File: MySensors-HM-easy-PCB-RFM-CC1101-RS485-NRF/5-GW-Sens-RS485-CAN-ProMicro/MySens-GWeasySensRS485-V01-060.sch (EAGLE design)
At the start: 28 parts, among them IC1 LM1117MPX-ADJ, IC2 LD117ADT50TR, IC6 LM1117MPX-ADJ, X4 1751264

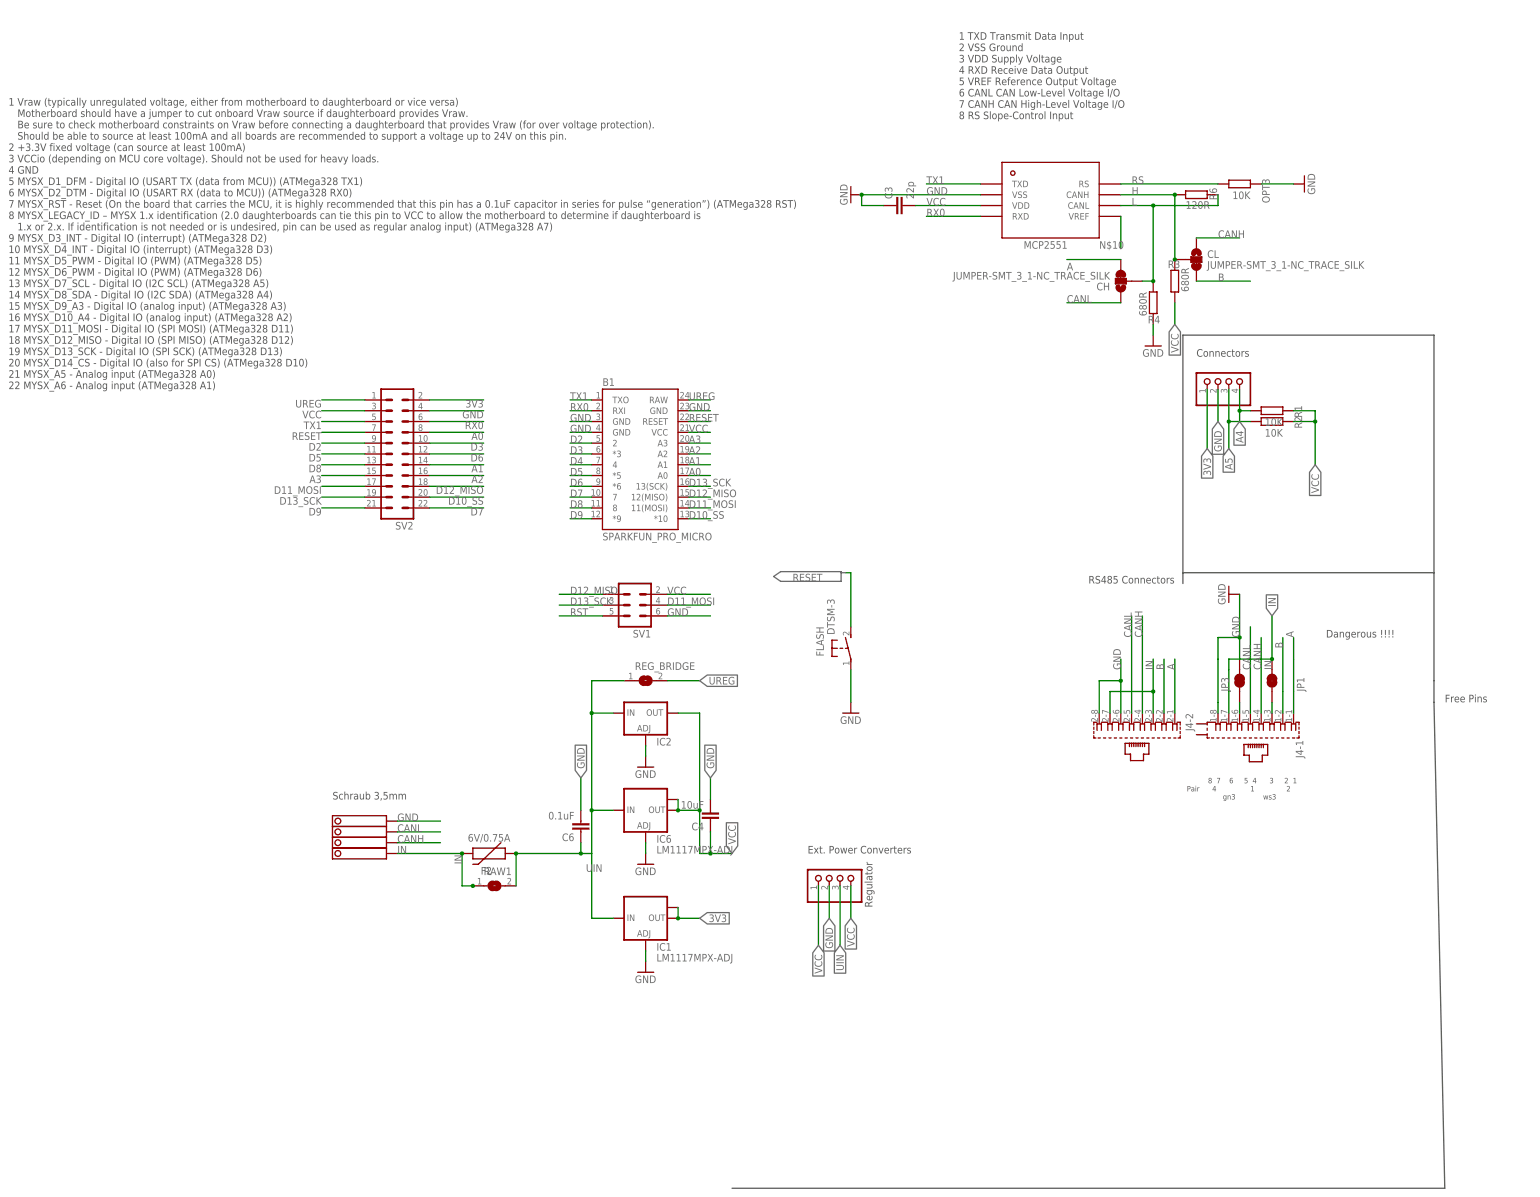
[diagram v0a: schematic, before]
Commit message: CAN/RS485 Board
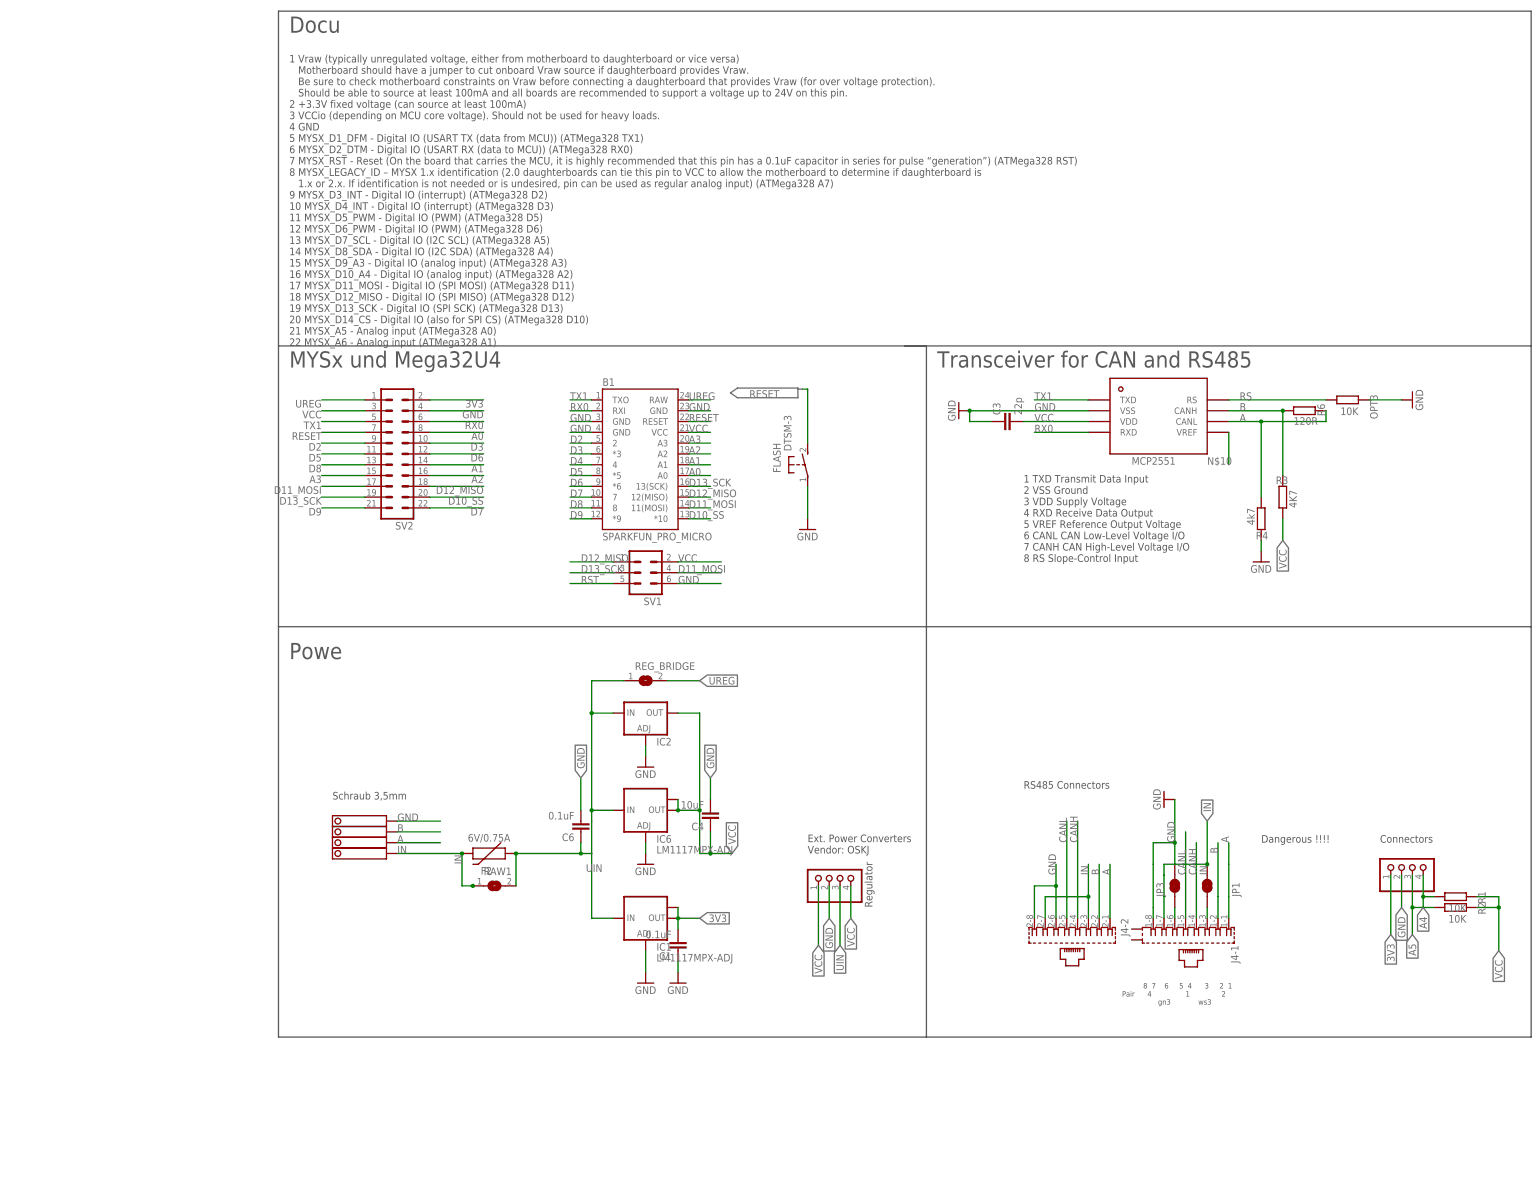
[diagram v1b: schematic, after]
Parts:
- removed CH, CL: JUMPER-SMT_3_1-NC_TRACE_SILK, SparkFun-Jumpers:JUMPER-SMT_3_1-NC_TRACE_SILK
- added C1: 0.1uF, rcl:C-EUC1206
- J4: device RJ45:RJ45_2X_NARROW_SHILDPINS_NOCASE -> RJ45:RJ45_2X_S
- R3: value 680R -> 4K7
- R4: value 680R -> 4k7
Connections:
- removed net H: CL.2, R3.2, R6.1, U$1.CANH
- removed net L: CH.2, R4.1, R6.2, U$1.CANL
- net 3V3: now also C1.2
- net A: now also R4.1, R6.2, U$1.CANL, X4-2.K; no longer CH.3
- net B: now also R3.2, R6.1, U$1.CANH, X4-3.K; no longer CL.3
- net CANH: no longer CL.1, X4-2.K
- net CANL: no longer CH.1, X4-3.K
- net GND: now also C1.1
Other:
- note added: "Docu"
- note added: "Ext. Power Converters Vendor: OSKJ"
- note added: "MYSx und Mega32U4"
- note added: "Powe"
- note added: "Transceiver for CAN and RS485"
- note removed: "Ext. Power Converters"
- note removed: "Free Pins"
- moved on the sheet: C3, FLASH, J4-1, J4-2, JP1, JP3, OPT3, R1, R2, R3, R4, R6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
